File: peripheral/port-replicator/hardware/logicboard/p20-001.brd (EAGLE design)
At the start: 72 x 72 mm, 21 parts, among them IC1 74LS07N, J0 DC9V, J1 AUDIO_JACK_3.5MM_PTH, J11 DIN5, J12 DIN5, J13 DIN5, J2 AUDIO_JACK_3.5MM_PTH, J3 AUDIO_JACK_3.5MM_PTH, J4 AUDIO_JACK_3.5MM_PTH

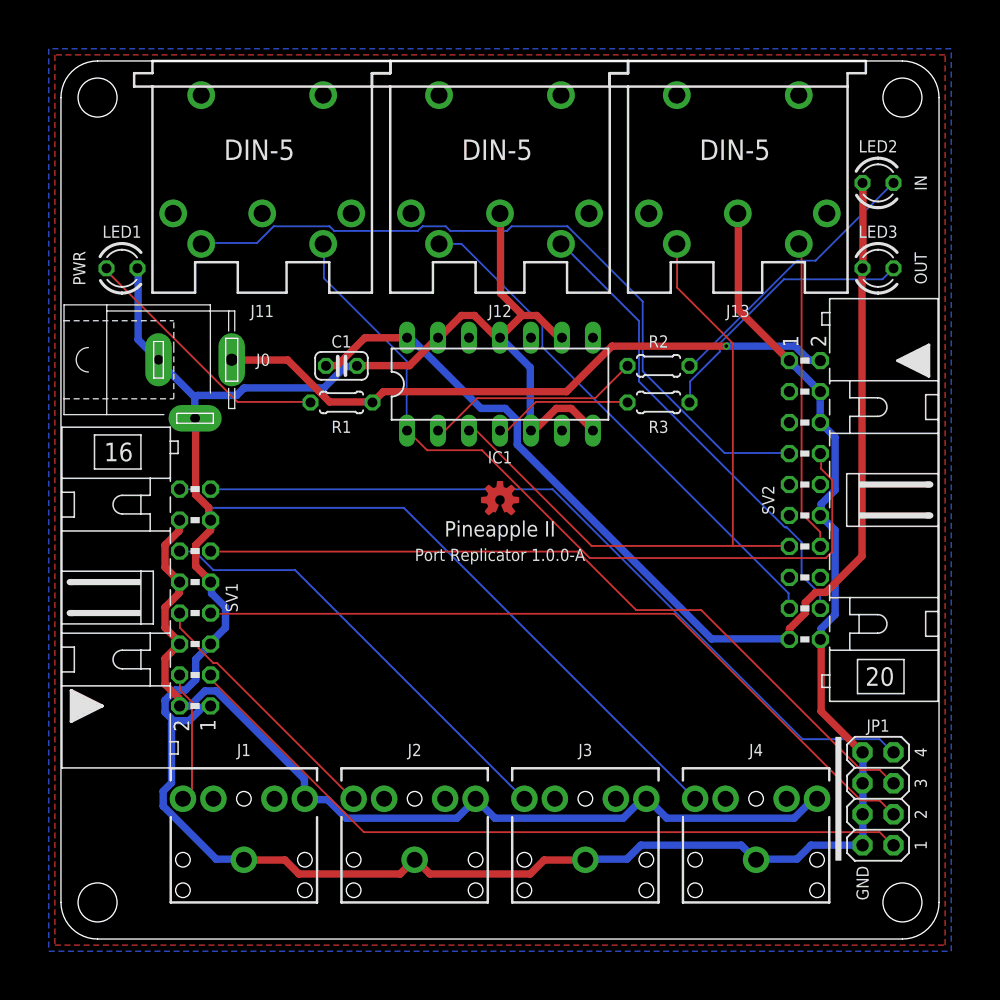
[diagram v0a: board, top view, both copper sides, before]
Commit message: The port replicator now has euroblock terminal.
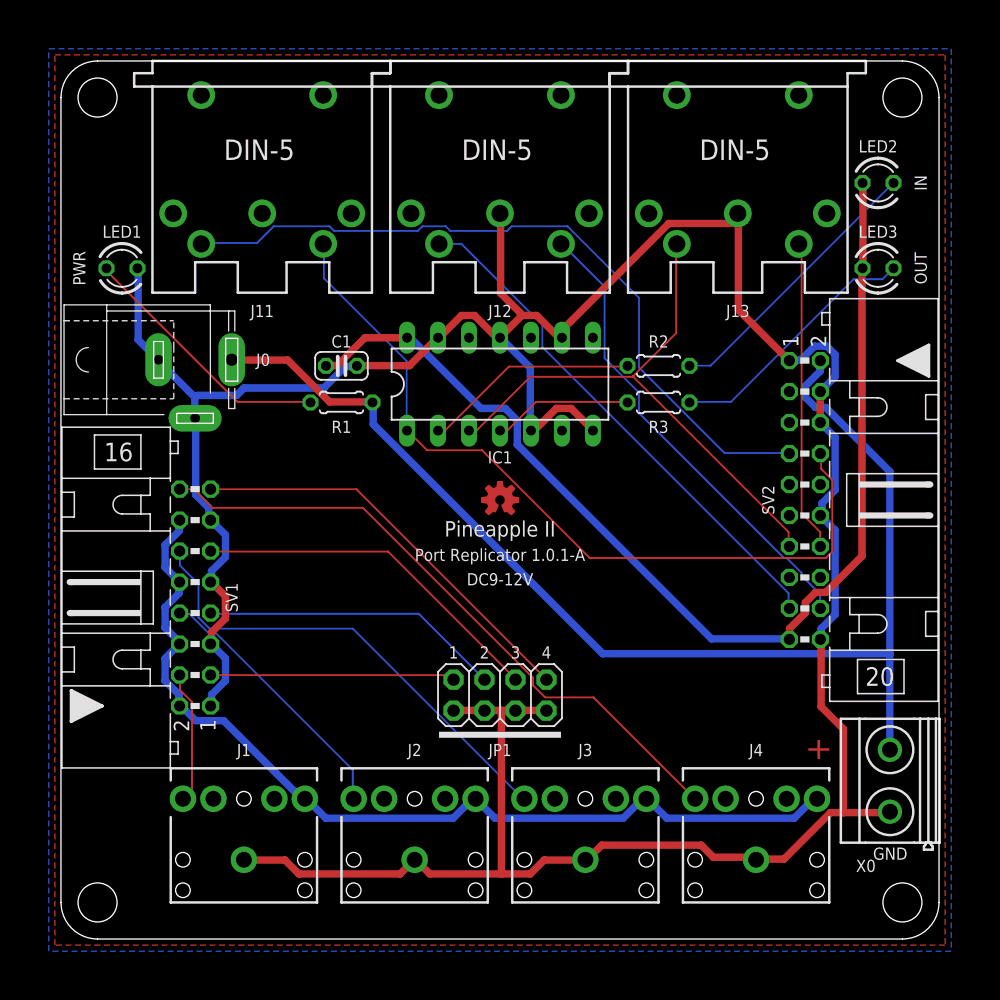
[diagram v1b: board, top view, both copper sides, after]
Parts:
- added X0: MKDSN1,5/2-5,08, con-phoenix-508:MKDSN1,5/2-5,08
- moved JP1 32.1 mm to (36.0, 20.0), turned to 0 degrees
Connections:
- net DTCT1: now also JP1.2; no longer JP1.1
- net DTCT2: now also JP1.4; no longer JP1.3
- net DTCT3: now also JP1.6; no longer JP1.5
- net DTCT4: now also JP1.8; no longer JP1.7
- net GND: now also JP1.1, JP1.3, JP1.5, JP1.7, X0.1; no longer JP1.2, JP1.4, JP1.6, JP1.8
- net V+: now also X0.2
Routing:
- net V+: track 52.1 -> 100.8 mm, vias 1 -> 0
- net DTCT1: track 62.0 -> 20.1 mm
- net DTCT2: track 62.8 -> 24.7 mm
- net DTCT3: track 63.9 -> 29.4 mm
- net DTCT4: track 64.9 -> 34.0 mm
- net GND: track 235.1 -> 258.1 mm
- net MOSND: track 56.9 -> 46.9 mm
- net ANLG3R: track 36.7 -> 39.0 mm
- net VCC/2: track 79.6 -> 77.6 mm
- net MOLED: track 22.7 -> 21.3 mm
- net ANLG2R: track 21.4 -> 22.0 mm
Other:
- board text added: "+"
- board text added: "Port Replicator 1.0.1-A"
- board text removed: "Port Replicator 1.0.0-A"

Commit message: Renewal of Port Replicator.
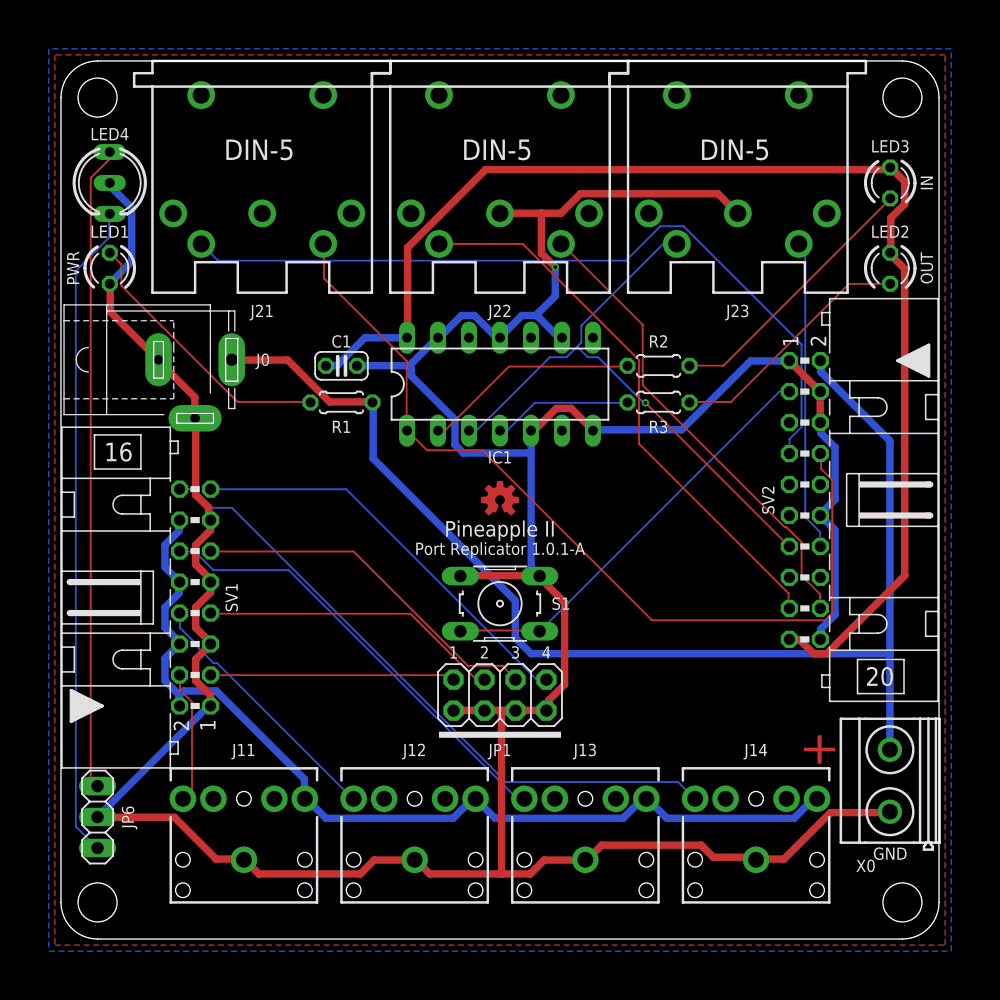
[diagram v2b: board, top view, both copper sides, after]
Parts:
- removed J1, J2, J3: AUDIO_JACK_3.5MM_PTH, SparkFun-Connectors:AUDIO-JACK
- added J21, J22, J23: DIN5, SparkFun-Connectors:DIN5-RA-PTH
- added JP6: (no value), pinhead:1X03
- added LED4: (no value), led:DUOLED-C-5MM
- added S1: (no value), switch-omron:B3F-10XX
- J11, J12, J13: value DIN5 -> AUDIO_JACK_3.5MM_PTH; device SparkFun-Connectors:DIN5-RA-PTH -> SparkFun-Connectors:AUDIO-JACK
- LED2: value IN -> OUT
- LED3: value OUT -> IN
- moved J13 66.7 mm to (43.0, 6.50), turned to 90 degrees
- moved J12 65.9 mm to (29.0, 6.50), turned to 90 degrees
- moved J11 65.5 mm to (15.0, 6.50), turned to 90 degrees
- moved LED2 7.07 mm to (68.0, 55.0), turned to 270 degrees
- moved LED3 7.07 mm to (68.0, 62.0), turned to 270 degrees
- moved LED1 1.00 mm to (4.00, 55.0), turned to 270 degrees
- renumbered J4 to J14
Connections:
- new net LED0: JP6.1, LED4.AR
- new net LED1: JP6.3, LED4.AX
- net ANLG1R: now also J11.RING; no longer J1.RING
- net ANLG2R: now also J12.RING; no longer J2.RING
- net ANLG3R: now also J13.RING; no longer J3.RING
- net GND: now also J11.SLEEVE, J12.SLEEVE, J13.SLEEVE, J22.2, J23.2, JP6.2, LED4.C, S1.1, S1.2; no longer J1.SLEEVE, J12.2, J13.2, J2.SLEEVE, J3.SLEEVE
- net MILED: now also LED3.K; no longer LED2.K
- net MIRTN: now also J21.5; no longer J11.5
- net MISND: now also J21.4; no longer J11.4
- net MOLED: now also LED2.K; no longer LED3.K
- net MORTN: now also J23.5; no longer J13.5
- net MOSND: now also J23.4; no longer J13.4
- net MTRTN: now also J22.5; no longer J12.5
- net MTSND: now also J22.4; no longer J12.4
- net RST: now also S1.3, S1.4
- net VCC/2: now also J11.TIP, J12.TIP, J13.TIP; no longer J1.TIP, J2.TIP, J3.TIP
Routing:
- net LED0: track 0.00 -> 53.9 mm
- net LED1: track 0.00 -> 52.9 mm
- net GND: track 258.1 -> 303.7 mm, vias 0 -> 1
- net RST: track 0.00 -> 35.2 mm
- net VCC: track 90.8 -> 104.8 mm
- net MIRTN: track 66.1 -> 73.2 mm
- net MISND: track 60.6 -> 64.3 mm
- net MTSND: track 42.9 -> 45.8 mm
- net ANLG3R: track 39.0 -> 36.7 mm
- net V+: track 100.8 -> 102.7 mm
- net VCC/2: track 77.6 -> 79.2 mm
- net MOSND: track 46.9 -> 48.4 mm, vias 0 -> 1
- net N$4: track 21.4 -> 22.6 mm
- net MOLED: track 21.3 -> 20.5 mm
- net MILED: track 22.9 -> 22.2 mm
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
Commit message: Silk.
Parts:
- removed LED1: PWR, led:LED3MM
- added LED0/1: (no value), led:DUOLED-C-5MM
- LED2: value OUT -> IN
- LED3: value IN -> OUT
- LED4: value (none) -> PWR; device led:DUOLED-C-5MM -> led:LED3MM
- moved LED3 7.07 mm to (69.0, 55.0), turned to 90 degrees
- moved LED4 7.07 mm to (3.00, 55.0), turned to 90 degrees
- moved LED2 5.82 mm to (69.0, 60.7), turned to 90 degrees
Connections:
- removed net MILED: LED3.K, R2.2
- removed net MOLED: LED2.K, R3.2
- removed net N$4: LED1.A, R1.1
- new net LEDMI: LED2.K, R2.2
- new net LEDMO: LED3.K, R3.2
- new net LEDPWR: LED4.A, R1.1
- net GND: now also LED0/1.C, LED4.K; no longer LED1.K, LED4.C
- net LED0: now also LED0/1.AR; no longer LED4.AR
- net LED1: now also LED0/1.AX; no longer LED4.AX
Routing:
- net LEDMI: track 0.00 -> 23.7 mm
- net N$4: track 22.6 -> 0.00 mm
- net LEDMO: track 0.00 -> 22.5 mm
- net MILED: track 22.2 -> 0.00 mm
- net LEDPWR: track 0.00 -> 21.5 mm
- net MOLED: track 20.5 -> 0.00 mm
- net MIRTN: track 73.2 -> 59.9 mm
- net GND: track 303.7 -> 294.3 mm, vias 1 -> 0
- net VCC: track 104.8 -> 96.8 mm
- net MISND: track 64.3 -> 57.5 mm
- net MOSND: track 48.4 -> 53.8 mm, vias 1 -> 0
- net MTSND: track 45.8 -> 46.4 mm
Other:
- board text added: "0"
- board text added: "K"

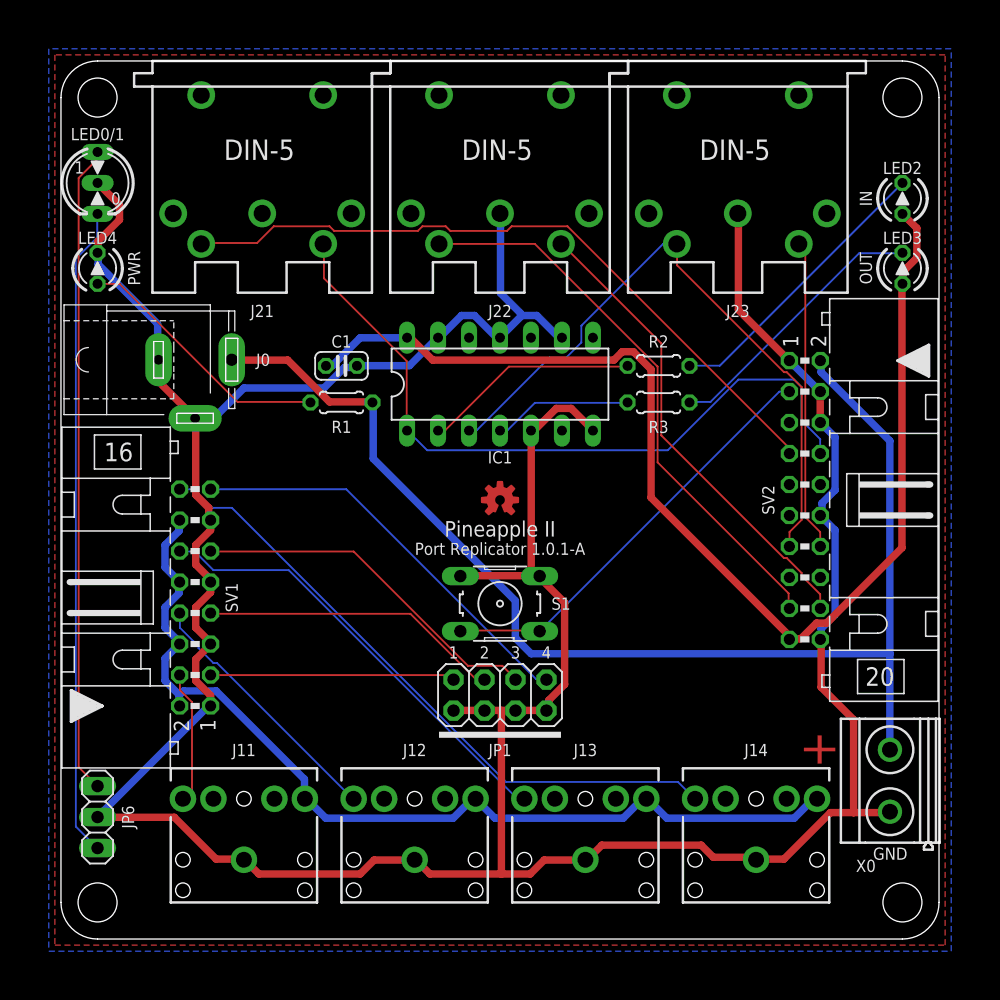
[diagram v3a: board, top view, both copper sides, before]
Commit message: Updated backside port to 2.0.
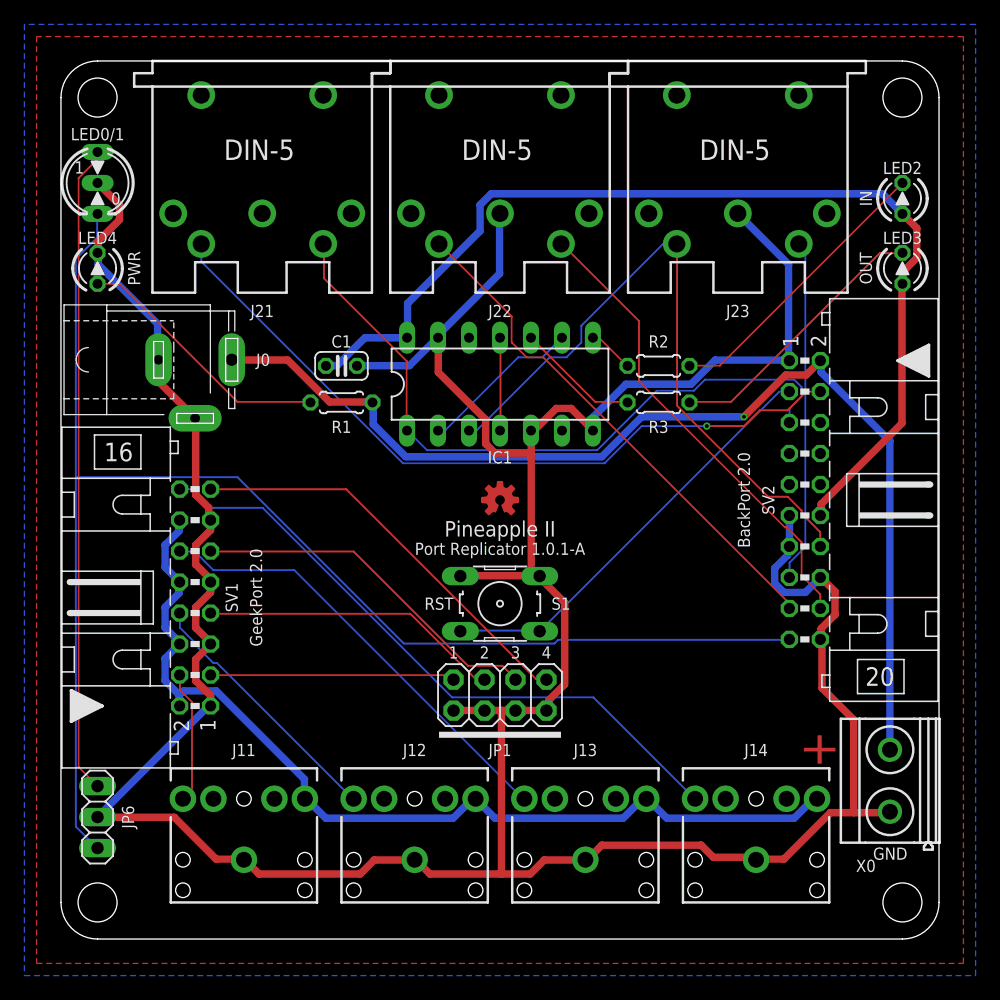
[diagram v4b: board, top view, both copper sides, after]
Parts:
- IC1: value 74LS07N -> 74ALS04N
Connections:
- removed net LED0A: SV2.5
- new net N$3: IC1.8, R2.1
- new net N$4: IC1.10, R3.1
- net GND: now also SV2.11, SV2.13, SV2.16; no longer IC1.11, IC1.9, SV2.12, SV2.4, SV2.6
- net LED0: now also SV2.19
- net MIRTN: now also SV2.5; no longer SV2.8
- net MISND: now also SV2.4; no longer SV2.7
- net MORTN: now also SV2.15; no longer SV2.14
- net MOSND: now also SV2.14; no longer SV2.13
- net MRX+: now also SV2.6; no longer SV2.9
- net MRX-: now also SV2.8; no longer SV2.11
- net MRXDTCT: now also SV2.7; no longer SV2.10
- net MTX+: now also SV2.9; no longer SV2.15
- net MTX-: now also SV2.10; no longer SV2.16
- net N$1: now also IC1.9; no longer R2.1
- net N$2: now also IC1.11; no longer R3.1
- net VCC: now also SV2.12; no longer SV2.19
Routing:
- net LED0: track 53.5 -> 117.8 mm
- net V+: track 102.7 -> 90.2 mm, vias 0 -> 1
- net VCC: track 96.8 -> 85.2 mm
- net N$4: track 0.00 -> 10.1 mm
- net N$1: track 17.8 -> 13.3 mm
- net MISND: track 57.5 -> 61.5 mm, vias 0 -> 1
- net MTSND: track 46.4 -> 42.6 mm
- net N$3: track 0.00 -> 3.79 mm
- net N$2: track 11.4 -> 7.67 mm
- net MIRTN: track 59.9 -> 57.2 mm
- net MORTN: track 25.5 -> 28.1 mm
- net MOSND: track 53.8 -> 54.8 mm
- net GND: track 294.3 -> 293.5 mm
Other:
- board text added: "BackPort 2.0"
- board text added: "GeekPort 2.0"
- board text added: "RST"
